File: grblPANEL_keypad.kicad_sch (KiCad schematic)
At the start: 48 parts, among them J601 Conn_02x10_Odd_Even, U601 ADP5589

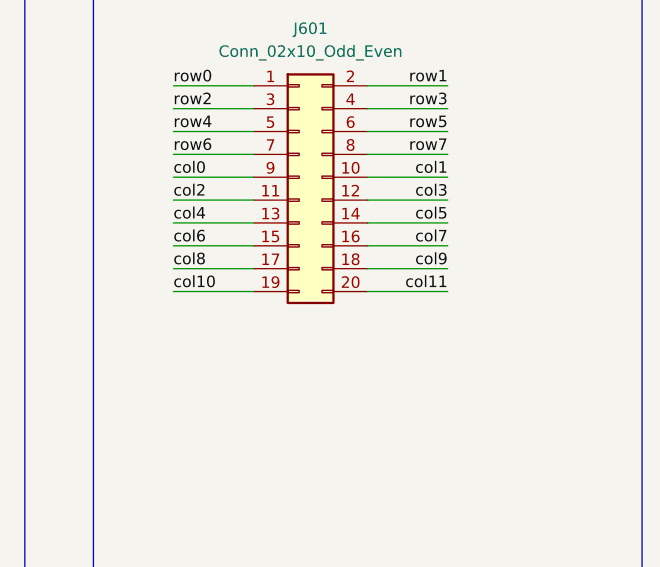
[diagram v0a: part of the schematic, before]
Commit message: ERC fixes
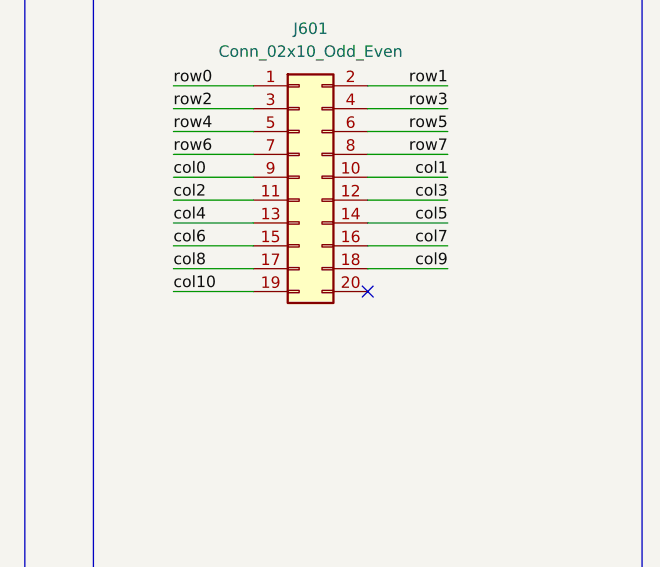
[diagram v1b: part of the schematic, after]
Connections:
- net col11: no longer names the net of J601.20 (Pin_20)
- no-connect marks 0 -> 1
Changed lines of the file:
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@@
   (junction (at 134.62 134.62) (diameter 0) (color 0 0 0 0)
   )
+  (no_connect (at 234.95 97.79))
   (wire (pts (xy 135.89 64.77) (xy 182.88 64.77))
     (stroke (width 0) (type default) (color 0 0 0 0))
@@
   )
   (wire (pts (xy 77.47 64.77) (xy 83.82 64.77))
-    (stroke (width 0) (type default) (color 0 0 0 0))
-  )
-  (wire (pts (xy 234.95 97.79) (xy 243.84 97.79))
     (stroke (width 0) (type default) (color 0 0 0 0))
   )
@@
     (effects (font (size 1.27 1.27)) (justify right bottom))
   )
-  (label "col11" (at 243.84 97.79 180)
-    (effects (font (size 1.27 1.27)) (justify right bottom))
-  )

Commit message: Refresh
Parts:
- C601: footprint (none) -> Capacitor_SMD:C_1206_3216Metric
- C602: value 0u1 -> 100n; footprint (none) -> Capacitor_SMD:C_0603_1608Metric
- D601, D602, D603, D604, D605, D606, D607, D608, D609, D610, D611, D612, D613, D614, D615, D616, D617, D618, D619: footprint (none) -> Diode_SMD:D_SOD-323
- J601: footprint (none) -> Connector_IDC:IDC-Header_2x10_P2.54mm_Vertical
- R601, R602, R603, R604, R605, R606, R607, R608, R609, R610, R611, R612, R613, R614, R615, R616, R617, R618, R619, R620, R621, R622, R623: footprint (none) -> Resistor_SMD:R_0603_1608Metric
- TP601, TP602: footprint (none) -> Connector_Pin:Pin_D1.0mm_L10.0mm
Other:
- note added: "Notes: Schematic loosely based on Digilent PmodIOXP breakout. 10k pull ups should be good for 100kHz I2C."
- note added: "todo: Find TVS packages with multiple channels?"
- note removed: "Notes: Confirm pull ups Use series resistors & transient protection?"
- note removed: "Use TVS packages with multiple channels?"
- moved on the sheet: C601, C602, R601, R602, R603, R604, TP601

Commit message: PCB layout - WIP
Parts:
- TP601, TP602: footprint Connector_Pin:Pin_D1.0mm_L10.0mm -> TestPoint:TestPoint_THTPad_D2.0mm_Drill1.0mm
- U601: footprint dresco:QFN-24-1EP_3.5x3.5mm_P0.4mm_EP2.2x2.2mm -> dresco:LFCSP-24-1EP_3.5x3.5mm_P0.4mm_EP2.2x2.2mm_ThermalVias
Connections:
- net R4: now reaches R609.1, U601.4 (R4)
- net R6: now reaches R611.1, U601.2 (R6)
- net KEYPAD_RST: now reaches R604.2, U601.17 (*RST)
- net C9: now reaches R622.1, U601.20 (C9)
- net R0: now reaches R605.1, U601.8 (R0)
- net R2: now reaches R607.1, U601.6 (R2)
- net C1: now reaches R614.1, U601.10 (C1)
- net R7: now reaches R612.1, U601.1 (R7)
- net C10: now reaches R623.1, U601.21 (C10)
- net C2: now reaches R615.1, U601.11 (C2)
- net C3: now reaches R616.1, U601.12 (C3)
- net C4: now reaches R617.1, U601.13 (C4)
- net C5: now reaches R618.1, U601.14 (C5)
- net C6: now reaches R619.1, U601.15 (C6)
- net C7: now reaches R620.1, U601.16 (C7)
- net C8: now reaches R621.1, U601.19 (C8)
- net KEYPAD_INT: now reaches R603.2, U601.24 (*INT)
- net R5: now reaches R610.1, U601.3 (R5)
- net R3: now reaches R608.1, U601.5 (R3)
- net R1: now reaches R606.1, U601.7 (R1)
- net C0: now reaches R613.1, U601.9 (C0)
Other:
- moved on the sheet: D601, D602, D603, D604, D605, D606, D607, D608, D609, D610, D611, D612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

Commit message: WIP layout
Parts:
- added D?: PESD3V3L4UF, Package_TO_SOT_SMD:SOT-886, symbol Power_Protection:PESD3V3L4UF
- added RN?: R_Pack04, symbol Device:R_Pack04
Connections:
- new net: D?.2 (A), D?.5 (A)
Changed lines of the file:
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@@
     (pin "1")
+  )
+  (symbol (lib_id "Power_Protection:PESD3V3L4UF") (at 236.22 118.11 0) (unit 1)
+    (in_bom yes) (on_board yes) (fields_autoplaced)
+    (property "Reference" "D?" (id 0) (at 236.22 111.76 0))
+    (property "Value" "PESD3V3L4UF" (id 1) (at 236.22 114.3 0))
+    (property "Footprint" "Package_TO_SOT_SMD:SOT-886" (id 2) (at 236.22 118.11 0)
+      (effects (font (size 1.27 1.27)) hide)
+    )
+    (property "Datasheet" "https://assets.nexperia.com/documents/data-sheet/PESDXL4UF_G_W.pdf" (id 3) (at 236.22 118.11 0)
+      (effects (font (size 1.27 1.27)) hide)
+    )
+    (pin "1")
+    (pin "2")
+    (pin "5")
+    (pin "3")
+    (pin "4")
+    (pin "6")
   )
   (symbol (lib_id "Device:R") (at 43.18 68.58 0) (unit 1)
@@
     (pin "1")
   )
+  (symbol (lib_id "Device:R_Pack04") (at 118.11 142.24 270) (unit 1)
+    (in_bom yes) (on_board yes) (fields_autoplaced)
+    (property "Reference" "RN?" (id 0) (at 118.11 130.81 90))
+    (property "Value" "R_Pack04" (id 1) (at 118.11 133.35 90))
+    (property "Footprint" "" (id 2) (at 118.11 149.225 90)
+      (effects (font (size 1.27 1.27)) hide)
+    )
+    (property "Datasheet" "~" (id 3) (at 118.11 142.24 0)
+      (effects (font (size 1.27 1.27)) hide)
+    )
+    (pin "1")
+    (pin "2")
+    (pin "3")
+    (pin "4")
+    (pin "5")
+    (pin "6")
+    (pin "7")
+    (pin "8")
+  )
   (symbol (lib_id "Device:D_TVS") (at 146.05 120.65 90) (unit 1)

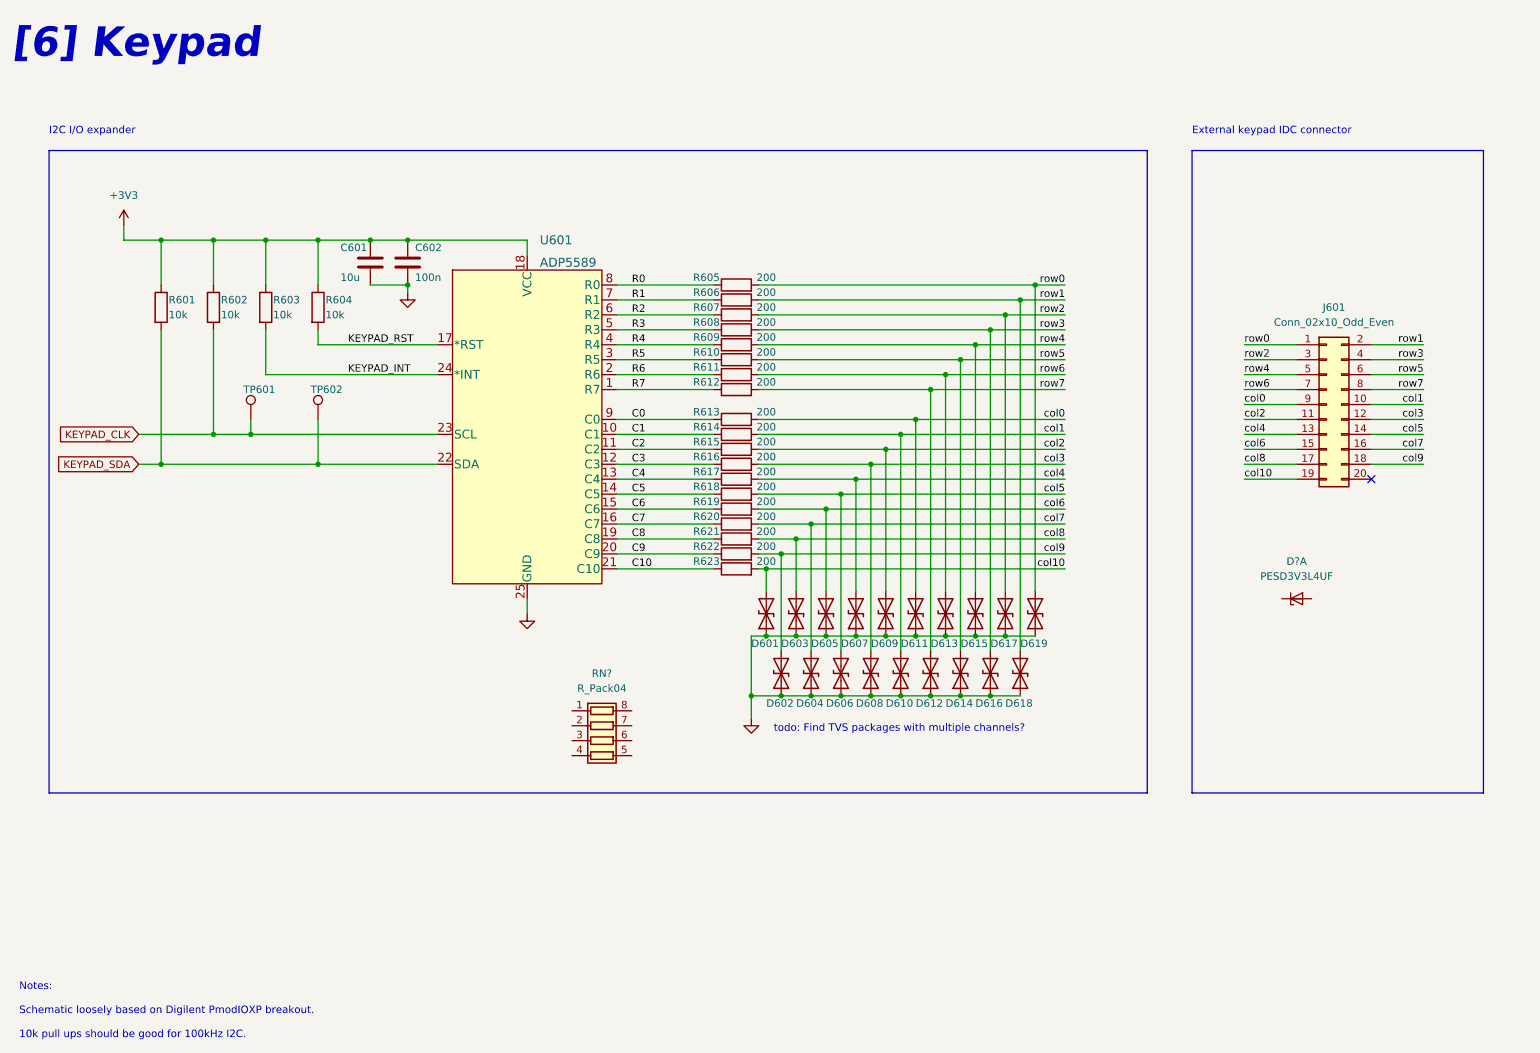
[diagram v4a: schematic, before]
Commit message: Resistor & TVS arrays
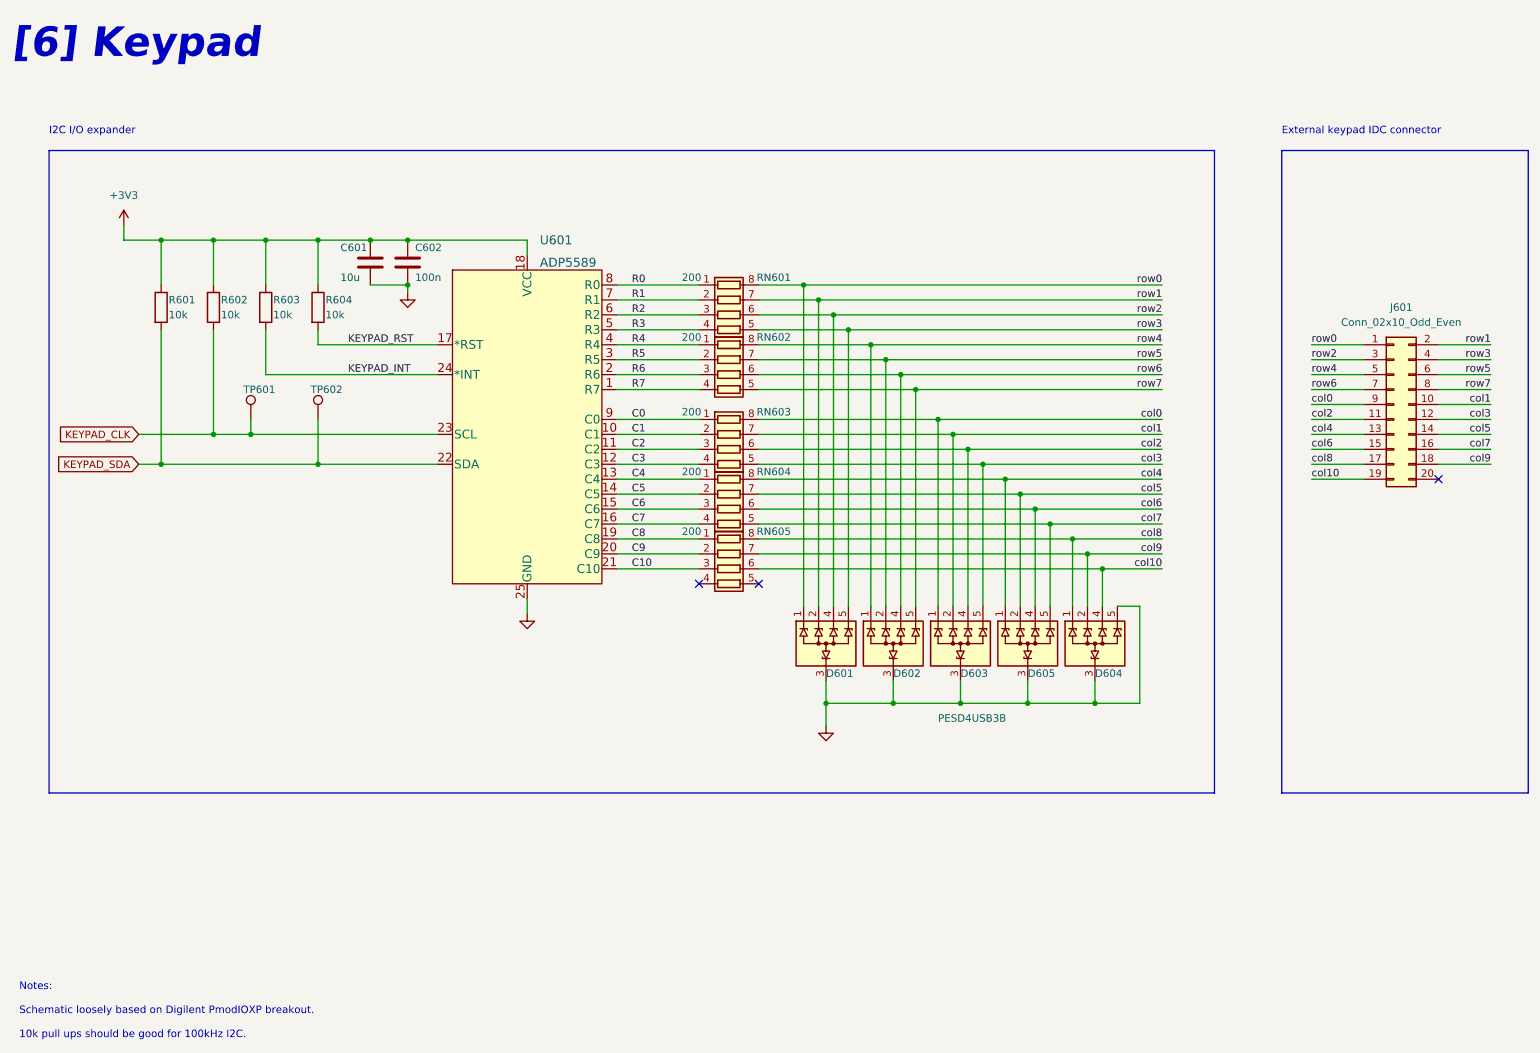
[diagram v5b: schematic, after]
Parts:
- removed D601, D602, D603, D604, D605, D606, D607, D608, D609, D610, D611, D612, D613, D614, D615, D616, D617, D618, D619: D_TVS, Diode_SMD:D_SOD-323, symbol Device:D_TVS
- removed D?: PESD3V3L4UF, Package_TO_SOT_SMD:SOT-886, symbol Power_Protection:PESD3V3L4UF
- removed R605, R606, R607, R608, R609, R610, R611, R612, R613, R614, R615, R616, R617, R618, R619, R620, R621, R622, R623: 200, Resistor_SMD:R_0603_1608Metric, symbol Device:R
- added D601, D602, D603, D604, D605: PESD4USB3B, dresco:SOT1176D, symbol dresco:PESD4USB3B
- added RN602, RN603, RN604, RN605: 200, Resistor_SMD:R_Array_Concave_4x0603, symbol Device:R_Pack04
- RN601: renamed from RN?; value R_Pack04 -> 200; footprint (none) -> Resistor_SMD:R_Array_Concave_4x0603
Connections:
- net C0: now also RN603.1 (R1.1)
- net C1: now also RN603.2 (R2.1)
- net C10: now also RN605.3 (R3.1)
- net C2: now also RN603.3 (R3.1)
- net C3: now also RN603.4 (R4.1)
- net C4: now also RN604.1 (R1.1)
- net C5: now also RN604.2 (R2.1)
- net C6: now also RN604.3 (R3.1)
- net C7: now also RN604.4 (R4.1)
- net C8: now also RN605.1 (R1.1)
- net C9: now also RN605.2 (R2.1)
- net GND: now also D601.3 (GND), D601.8 (GND), D602.3 (GND), D602.8 (GND), D603.3 (GND), D603.8 (GND), D604.3 (GND), D604.8 (GND), D605.3 (GND), D605.5 (TVS4), D605.6 (TVS4), D605.8 (GND)
- net R0: now also RN601.1 (R1.1)
- net R1: now also RN601.2 (R2.1)
- net R2: now also RN601.3 (R3.1)
- net R3: now also RN601.4 (R4.1)
- net R4: now also RN602.1 (R1.1)
- net R5: now also RN602.2 (R2.1)
- net R6: now also RN602.3 (R3.1)
- net R7: now also RN602.4 (R4.1)
- net col0: now also D603.1 (TVS1), D603.10 (TVS1), RN603.8 (R1.2)
- net col1: now also D603.2 (TVS2), D603.9 (TVS2), RN603.7 (R2.2)
- net col10: now also D605.4 (TVS3), D605.7 (TVS3), RN605.6 (R3.2)
- net col2: now also D603.4 (TVS3), D603.7 (TVS3), RN603.6 (R3.2)
- net col3: now also D603.5 (TVS4), D603.6 (TVS4), RN603.5 (R4.2)
- net col4: now also D604.1 (TVS1), D604.10 (TVS1), RN604.8 (R1.2)
- net col5: now also D604.2 (TVS2), D604.9 (TVS2), RN604.7 (R2.2)
- net col6: now also D604.4 (TVS3), D604.7 (TVS3), RN604.6 (R3.2)
- net col7: now also D604.5 (TVS4), D604.6 (TVS4), RN604.5 (R4.2)
- net col8: now also D605.1 (TVS1), D605.10 (TVS1), RN605.8 (R1.2)
- net col9: now also D605.2 (TVS2), D605.9 (TVS2), RN605.7 (R2.2)
- net row0: now also RN601.8 (R1.2), D601.1 (TVS1), D601.10 (TVS1)
- net row1: now also RN601.7 (R2.2), D601.2 (TVS2), D601.9 (TVS2)
- net row2: now also RN601.6 (R3.2), D601.4 (TVS3), D601.7 (TVS3)
- net row3: now also RN601.5 (R4.2), D601.5 (TVS4), D601.6 (TVS4)
- net row4: now also D602.1 (TVS1), D602.10 (TVS1), RN602.8 (R1.2)
- net row5: now also D602.2 (TVS2), D602.9 (TVS2), RN602.7 (R2.2)
- net row6: now also D602.4 (TVS3), D602.7 (TVS3), RN602.6 (R3.2)
- net row7: now also D602.5 (TVS4), D602.6 (TVS4), RN602.5 (R4.2)
- no-connect marks 1 -> 3
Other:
- note removed: "todo: Find TVS packages with multiple channels?"
- moved on the sheet: J601, RN601
